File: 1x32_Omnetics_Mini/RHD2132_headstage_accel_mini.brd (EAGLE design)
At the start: 160 x 100 mm, 18 parts, among them U1 RHD2132_QFN, U2 ADXL335

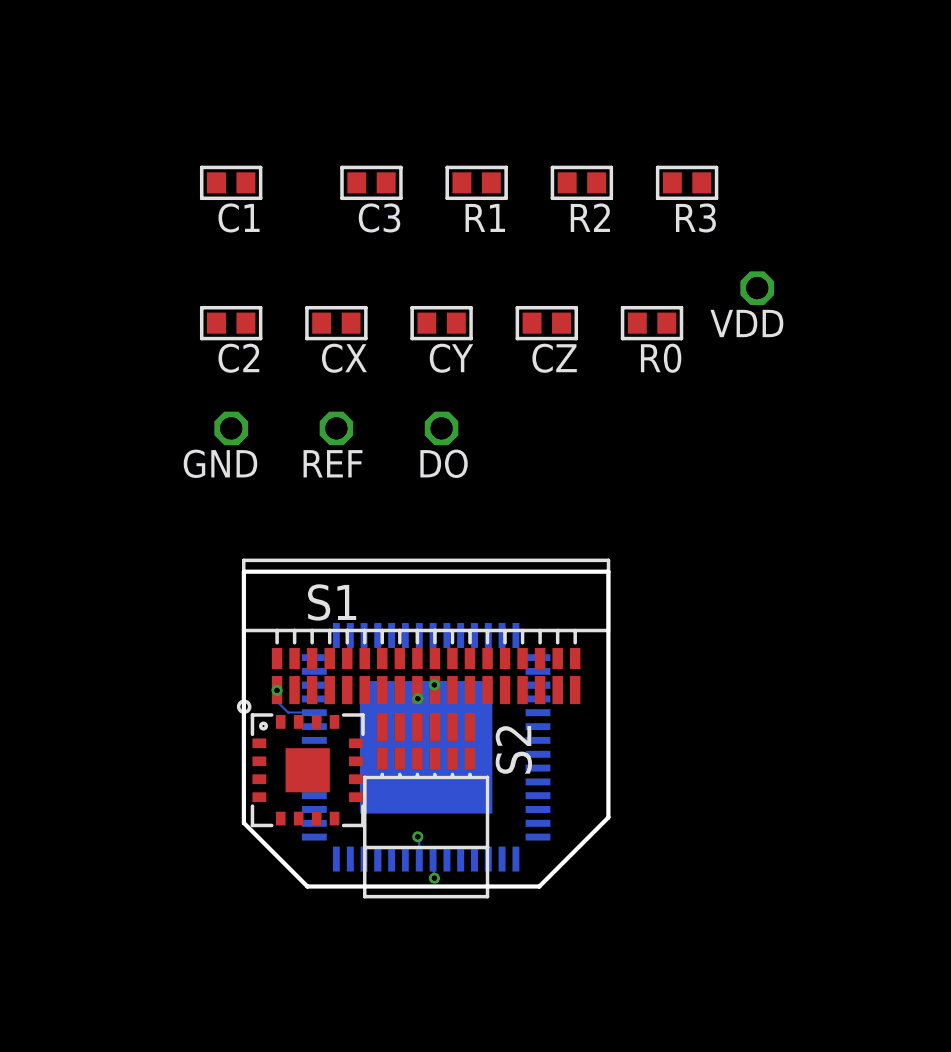
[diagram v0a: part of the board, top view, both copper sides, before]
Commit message: started some routing
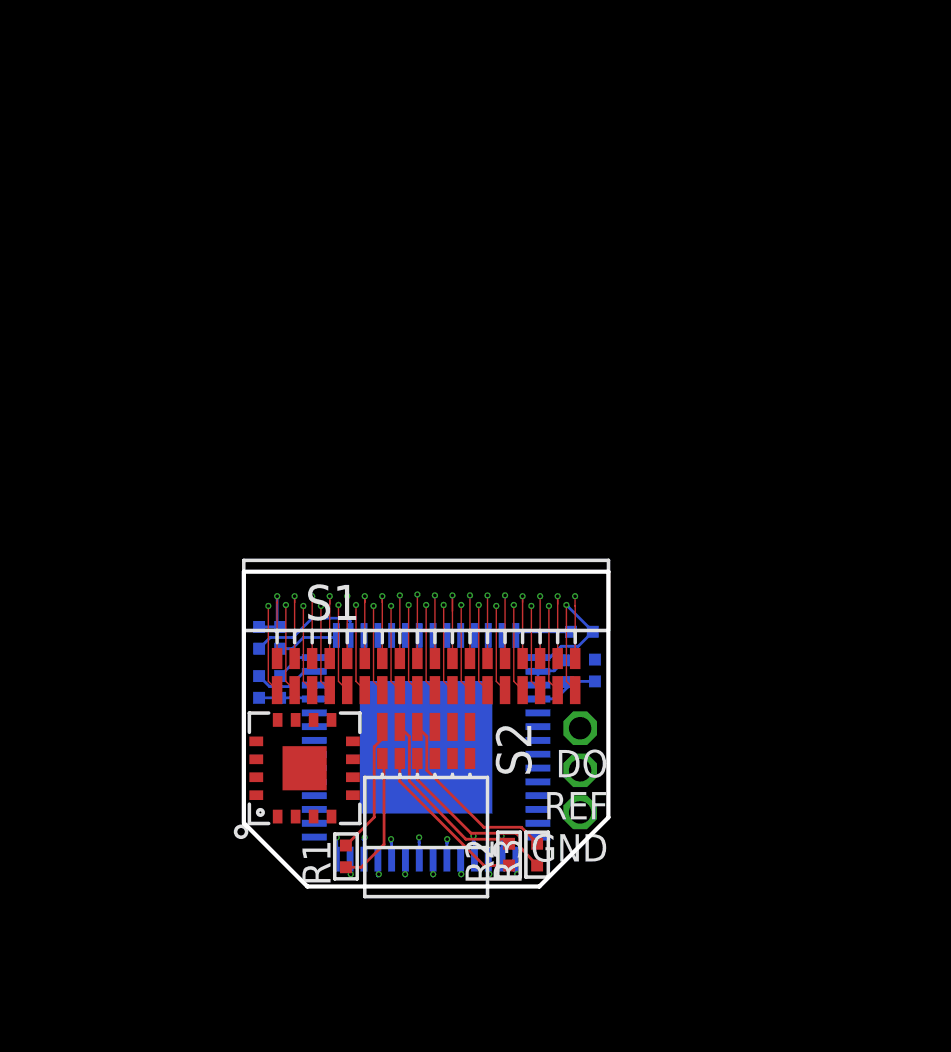
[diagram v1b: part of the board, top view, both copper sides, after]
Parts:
- removed VDD: TESTPOINT_SMALL, RHD2000_eval_board:TESTPOINT_SMALL
- C1, C2, C3, CX, CY, CZ, R0, R1, R2, R3: device RHD2000_eval_board:0402 -> RHD2000_eval_board:0201
- moved R3 24.9 mm to (92.9, 44.0), turned to 90 degrees
- moved R1 24.8 mm to (86.0, 43.9), turned to 90 degrees
- moved R2 24.5 mm to (91.9, 44.0), turned to 90 degrees
- moved C1 21.5 mm to (94.0, 50.6), flipped to the bottom, turned to 270 degrees
- moved GND 18.8 mm to (94.5, 45.5)
- moved C3 18.7 mm to (82.8, 50.0), flipped to the bottom, turned to 270 degrees
- moved C2 16.9 mm to (94.5, 52.0), flipped to the bottom
- moved CZ 15.4 mm to (82.8, 51.8), flipped to the bottom, turned to 90 degrees
- moved REF 15.2 mm to (94.5, 47.0)
- moved CX 13.3 mm to (83.6, 50.0), flipped to the bottom, turned to 270 degrees
- moved CY 12.8 mm to (83.6, 51.8), flipped to the bottom, turned to 90 degrees
- moved R0 12.7 mm to (95.0, 50.6), flipped to the bottom, turned to 90 degrees
- moved DO 12.0 mm to (94.5, 48.5)
- moved U2 0.13 mm to (84.5, 47.1), turned to 90 degrees
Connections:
- net VCC: no longer VDD.1
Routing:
- net GND: track 0.00 -> 16.0 mm, vias 0 -> 2
- net N$25: track 0.00 -> 14.2 mm, vias 0 -> 2
- net N$23: track 0.00 -> 13.9 mm, vias 0 -> 2
- net N$32: track 0.00 -> 13.9 mm, vias 0 -> 2
- net N$28: track 0.00 -> 13.8 mm, vias 0 -> 2
- net N$20: track 0.00 -> 13.8 mm, vias 0 -> 2
- net N$30: track 0.00 -> 13.6 mm, vias 0 -> 2
- net N$24: track 0.00 -> 13.0 mm, vias 0 -> 2
- net N$22: track 0.00 -> 12.9 mm, vias 0 -> 2
- net N$27: track 0.00 -> 12.7 mm, vias 0 -> 2
- net N$21: track 0.00 -> 12.6 mm, vias 0 -> 2
- net N$31: track 0.00 -> 12.6 mm, vias 0 -> 2
- net N$29: track 0.00 -> 12.5 mm, vias 0 -> 2
- net N$39: track 0.00 -> 6.86 mm
- net N$37: track 0.00 -> 6.67 mm
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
